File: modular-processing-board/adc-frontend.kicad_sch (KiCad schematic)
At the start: 81 parts, among them J1001 BWU.FL-IPEX1, J1002 BWU.FL-IPEX1, J1006 BWU.FL-IPEX1, J1008 BWU.FL-IPEX1, J601 Conn_Coaxial_Small, J602 BWU.FL-IPEX1, J603 BWU.FL-IPEX1, J604 Conn_Coaxial_Small, J605 BWU.FL-IPEX1, J606 BWU.FL-IPEX1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

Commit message: completed schematic
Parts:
- J601, J604: footprint Library:SMA_Amphenol_901-143_Vertical -> Connector_Coaxial:SMA_Amphenol_901-144_Vertical
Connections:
- net GND: now also J1001.2 (Ext)
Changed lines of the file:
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@@
 	)
 	(label "ADC_VOCM_BUFF"
-		(at 73.66 38.1 0)
-		(effects
-			(font
-				(size 1.27 1.27)
-			)
-			(justify left bottom)
-		)
-	)
-	(label "ADC_VOCM_BUFF"
 		(at 81.28 238.76 0)
 		(effects
@@
 			)
 		)
-		(property "Footprint" "Library:SMA_Amphenol_901-143_Vertical"
+		(property "Footprint" "Connector_Coaxial:SMA_Amphenol_901-144_Vertical"
 			(at 31.75 234.95 0)
 			(effects
@@
 		(dnp no)
 		(property "Reference" "J1001"
-			(at 63.5 94.4997 90)
+			(at 63.5 96.012 90)
 			(effects
 				(font
@@
 	)
 	(symbol
+		(lib_id "power:GND")
+		(at 60.96 91.44 0)
+		(mirror y)
+		(unit 1)
+		(exclude_from_sim no)
+		(in_bom yes)
+		(on_board yes)
+		(dnp no)
+		(property "Reference" "#PWR0623"
+			(at 60.96 97.79 0)
+			(effects
+				(font
+					(size 1.27 1.27)
+				)
+				(hide yes)
+			)
+		)
+		(property "Value" "GND"
+			(at 64.516 92.964 0)
+			(effects
+				(font
+					(size 1.27 1.27)
+				)
+			)
+		)
+		(property "Footprint" ""
+			(at 60.96 91.44 0)
+			(effects
+				(font
+					(size 1.27 1.27)
+				)
+				(hide yes)
+			)
+		)
+		(property "Datasheet" ""
+			(at 60.96 91.44 0)
+			(effects
+				(font
+					(size 1.27 1.27)
+				)
+				(hide yes)
+			)
+		)
+		(property "Description" "Power symbol creates a global label with name \"GND\" , ground"
+			(at 60.96 91.44 0)
+			(effects
+				(font
+					(size 1.27 1.27)
+				)
+				(hide yes)
+			)
+		)
+		(pin "1"
+		)
+		(instances
+			(project "modular-processing-board"
+				(path "/73b5a92f-908b-4f97-a96c-14ee20a7f293/f6ec5a2c-a447-41c5-b01d-0cfa4d0577c8"
+					(reference "#PWR0623")
+					(unit 1)
+				)
+			)
+		)
+	)
+	(symbol
 		(lib_id "power:VDDA")
 		(at 151.13 34.29 0)
@@
 		(dnp yes)
 		(property "Reference" "R1007"
-			(at 69.342 109.22 90)
+			(at 61.976 110.49 0)
 			(effects
 				(font
@@
 		)
 		(property "Value" "0"
-			(at 64.262 88.392 90)
+			(at 62.992 108.712 0)
 			(effects
 				(font
@@
 			)
 		)
-		(property "Footprint" "Library:SMA_Amphenol_901-143_Vertical"
+		(property "Footprint" "Connector_Coaxial:SMA_Amphenol_901-144_Vertical"
 			(at 40.64 125.73 0)
 			(effects

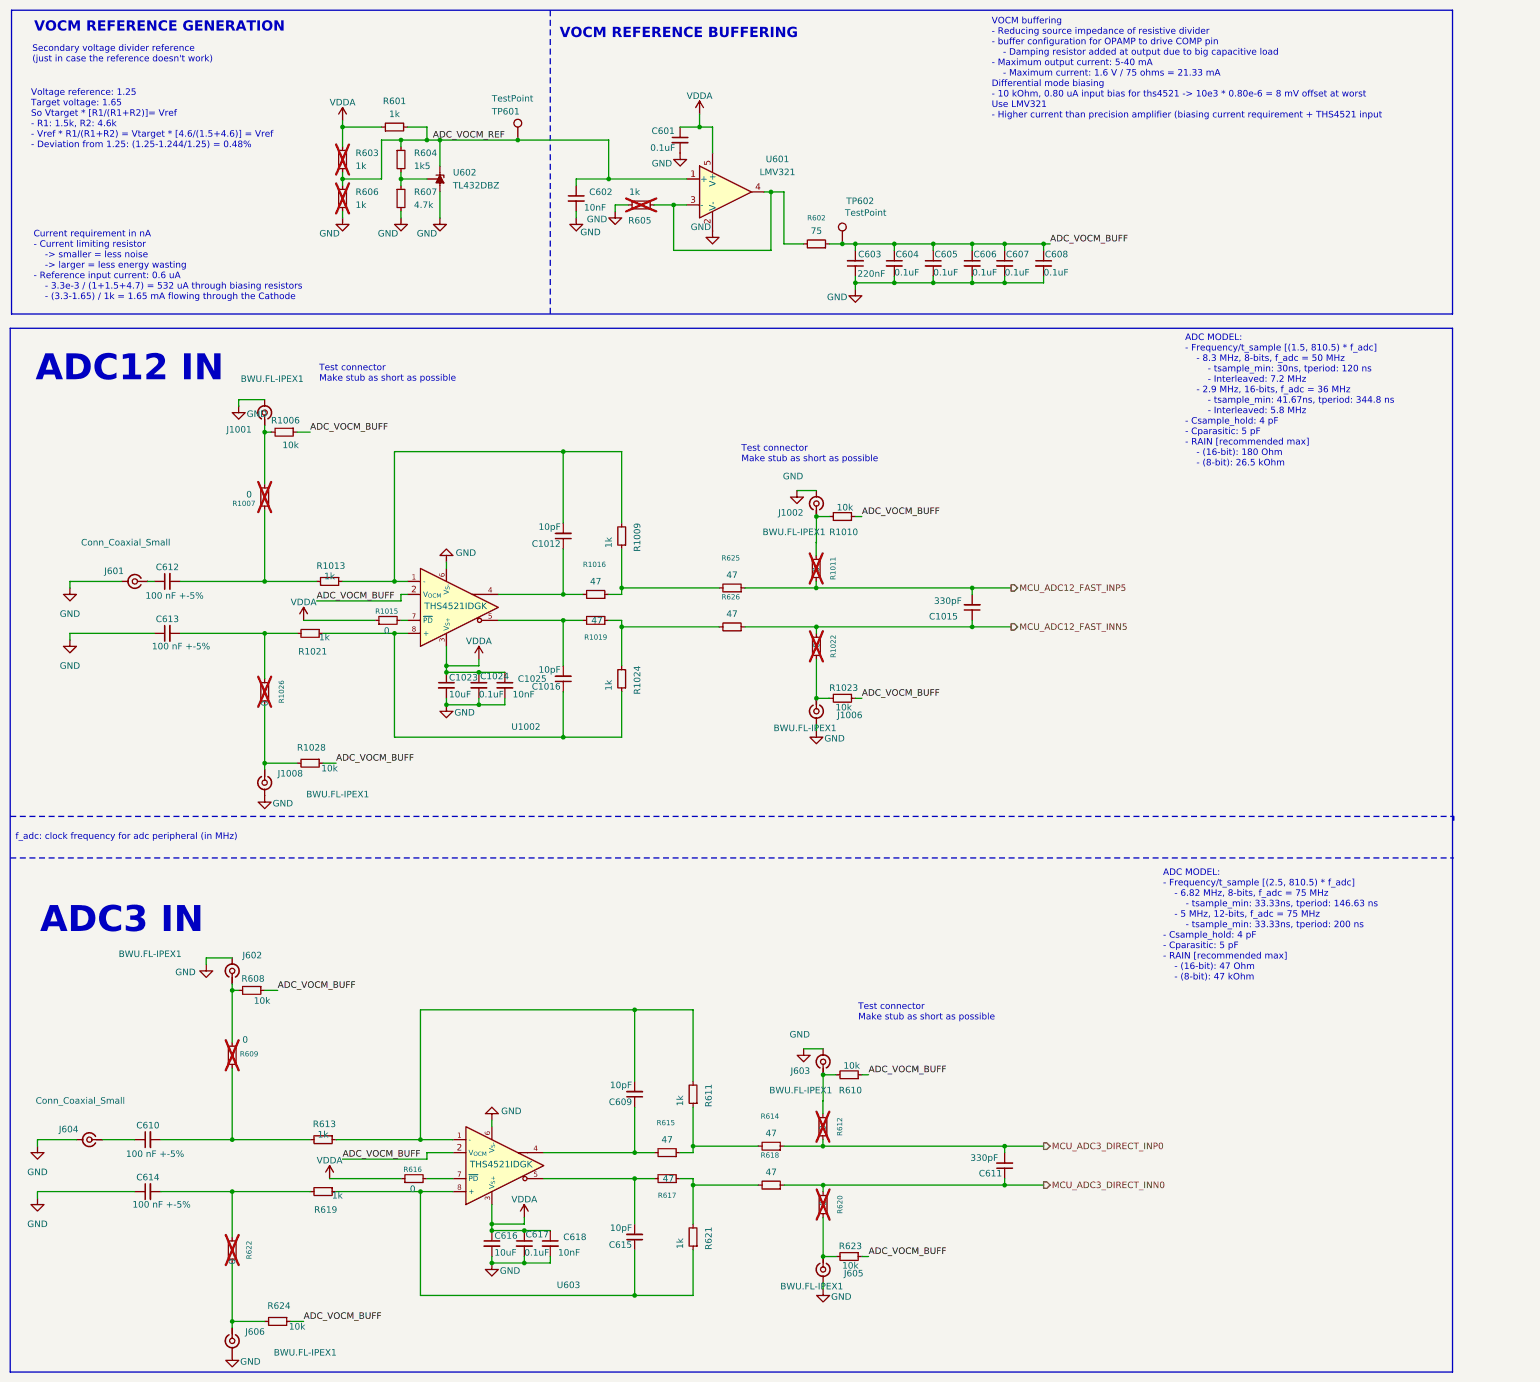
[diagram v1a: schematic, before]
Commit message: various changes to schematic (next) add bias resistors after testing results on acoustic-carrier-board
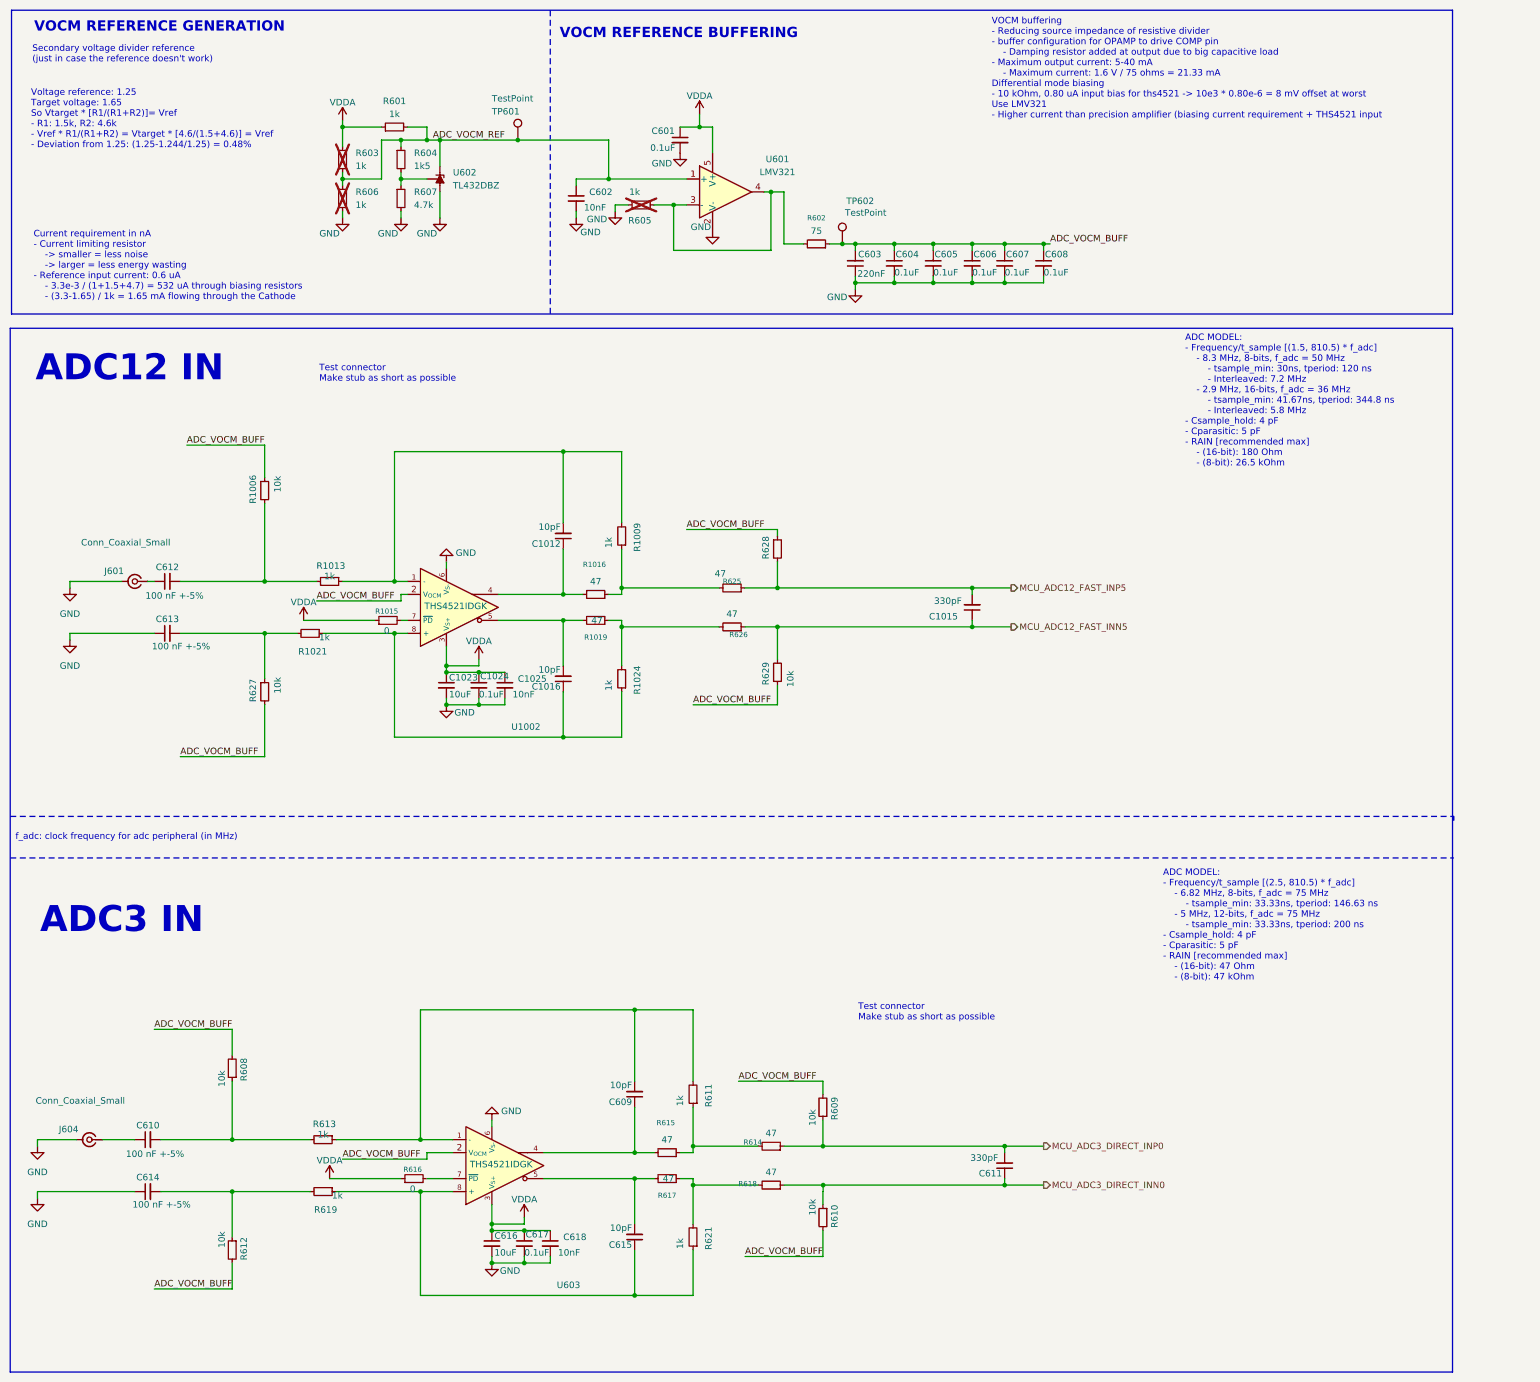
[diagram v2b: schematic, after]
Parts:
- removed J1001, J1002, J1006, J1008, J602, J603, J605, J606: BWU.FL-IPEX1, iw-connector:BWU.FL-IPEX1, symbol Connector:Conn_Coaxial_Small
- removed R1007, R1011, R1022, R1026, R620, R622: 0, Resistor_SMD:R_0603_1608Metric, symbol Device:R_Small
- removed R1010, R1023, R1028, R623, R624: 10k, Resistor_SMD:R_0603_1608Metric, symbol Device:R_Small
- added R627, R628, R629: 10k, Resistor_SMD:R_0603_1608Metric, symbol Device:R_Small
- C1024, C601, C604, C605, C606, C607, C608, C617: footprint Capacitor_SMD:C_0201_0603Metric -> Capacitor_SMD:C_0402_1005Metric; LPN (none) -> C307331; MPN (none) -> CL05B104KB54PNC
- R609, R612: value 0 -> 10k; LCSC Part Number C21189 -> C25804; Manufacturing Part Number 0603WAF0000T5E -> 0603WAF1002T5E; now fitted; now in the parts list
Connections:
- net ADC_VOCM_BUFF: now also R608.2, R609.2, R610.2, R612.2, R627.2, R628.1, R629.1; no longer R608.1, R610.1
- net MCU_ADC12_FAST_INN5: now also R629.2
- net MCU_ADC12_FAST_INP5: now also R628.2
- net MCU_ADC3_DIRECT_INP0: now also R609.1; no longer R612.1
- net at R1006.2: now also C612.2, R1013.2
- net at C614.2, R619.2: now also R612.1
- net at C613.2, R1021.2: now also R627.1
- net at C610.2, R613.2: now also R608.1; no longer R609.2
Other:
- moved on the sheet: R1006, R608

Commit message: started layout
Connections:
- net MCU_ADC3_DIRECT_INN0: now also R610.1
- net ADC12_IAMP-: now reaches C1012.2, R1009.2, R1013.1, U1002.1 (-)
- net ADC12_OAMP+: now reaches C1012.1, R1016.2, U1002.4
- net ADC12_OAMP-: now reaches C1016.2, R1019.2, U1002.5
- net ADC12_IAMP+: now reaches C1016.1, R1021.1, R1024.1, U1002.8 (+)
- net ADC3_OAMP+: now reaches C609.1, R615.2, U603.4
- net ADC3_IAMP+: now reaches C615.1, R619.1, R621.1, U603.8 (+)
- net ADC3_IAMP-: now reaches C609.2, R611.2, R613.1, U603.1 (-)
- net ADC3_OAMP-: now reaches C615.2, R617.2, U603.5
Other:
- moved on the sheet: R1013, R1021, R610

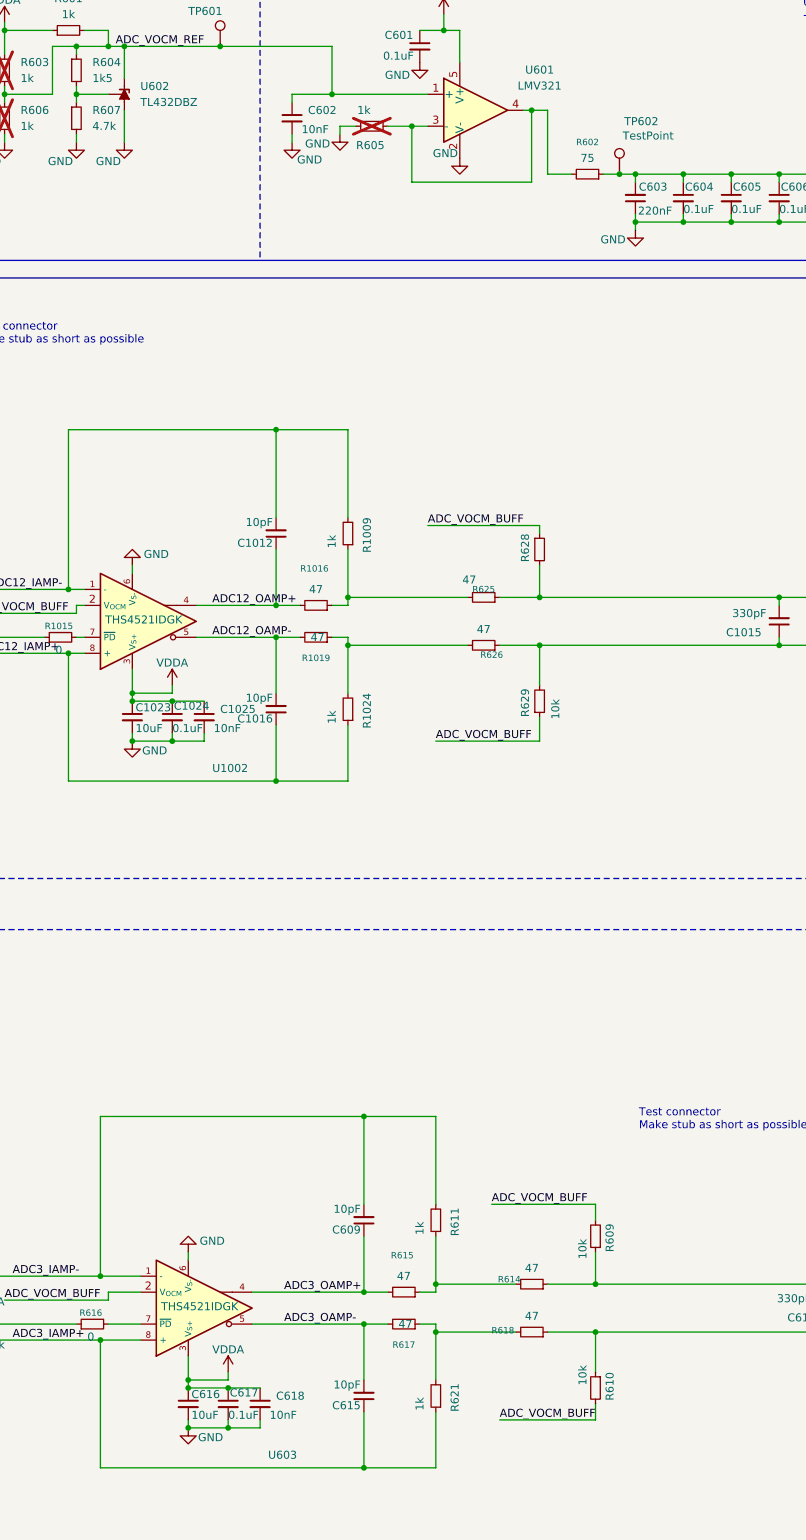
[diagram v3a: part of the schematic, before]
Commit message: removed power input jumpers to single one, added trace impedances and production restrictions (next) route sdram
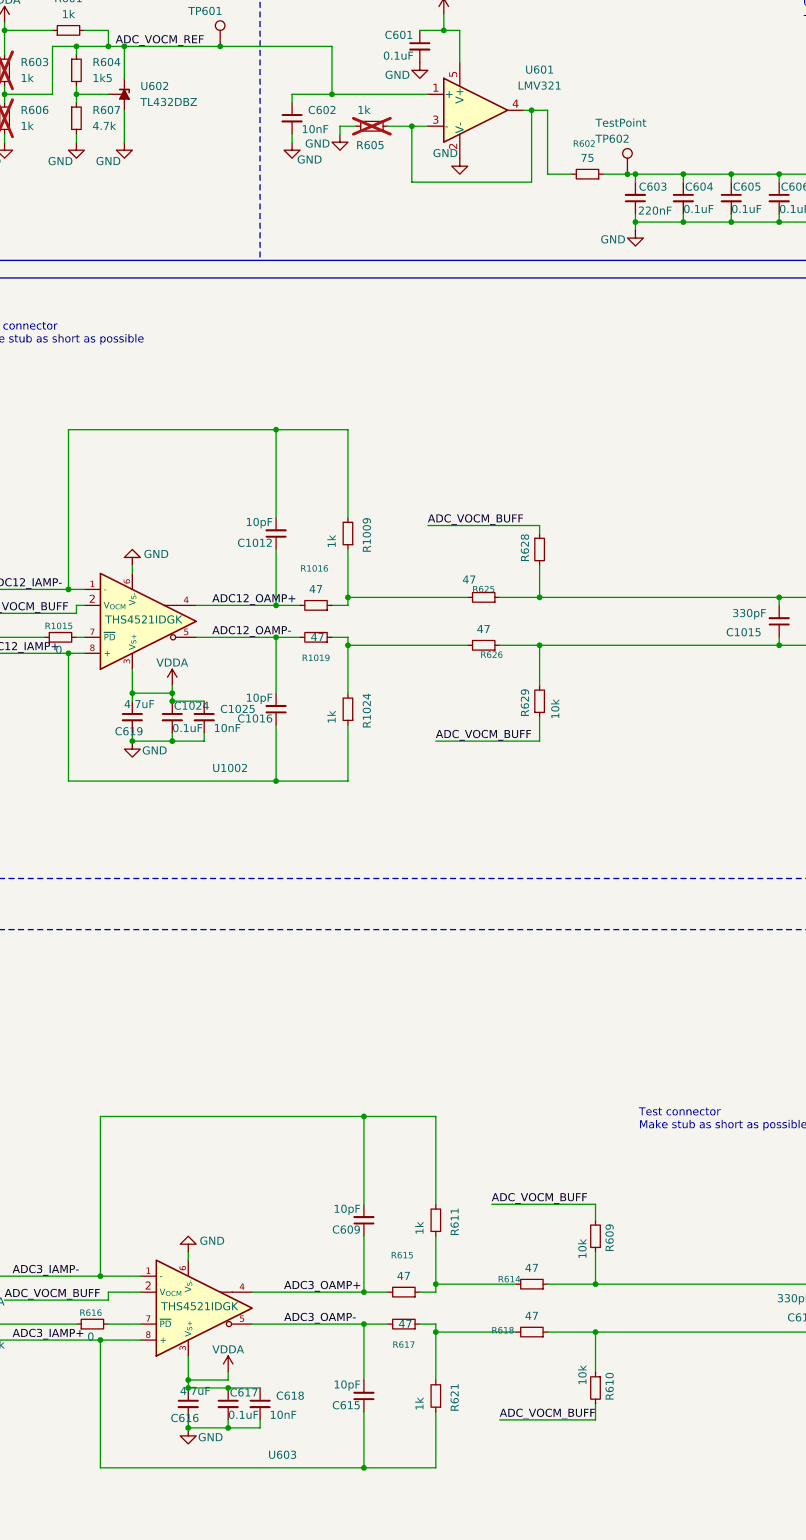
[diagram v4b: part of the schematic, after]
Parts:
- removed C1023: 10uF, Capacitor_SMD:C_0603_1608Metric, symbol Device:C_Small
- added C619: 4.7uF, Capacitor_SMD:C_0402_1005Metric, symbol Device:C_Small
- C616: value 10uF -> 4.7uF; footprint Capacitor_SMD:C_0603_1608Metric -> Capacitor_SMD:C_0402_1005Metric; LCSC Part Number C19702 -> C23733; Manufacturing Part Number CL10A106KP8NNNC -> CL05A475MP5NRNC
- TP601, TP602: footprint TestPoint:TestPoint_Loop_D1.80mm_Drill1.0mm_Beaded -> iw-misc:TestPoint_Pad_D0.5mm
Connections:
- net GND: now also C619.2
- net VDDA: now also C619.1
